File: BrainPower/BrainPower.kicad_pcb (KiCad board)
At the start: 2 copper layers, 149.9 x 111.3 mm, 10 parts, among them J1 BarrelJack_Horizontal, J2 PhoenixContact_MCV_1,5_2-G-5.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, P1 Golden finger, PCIeX1, Dual, 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

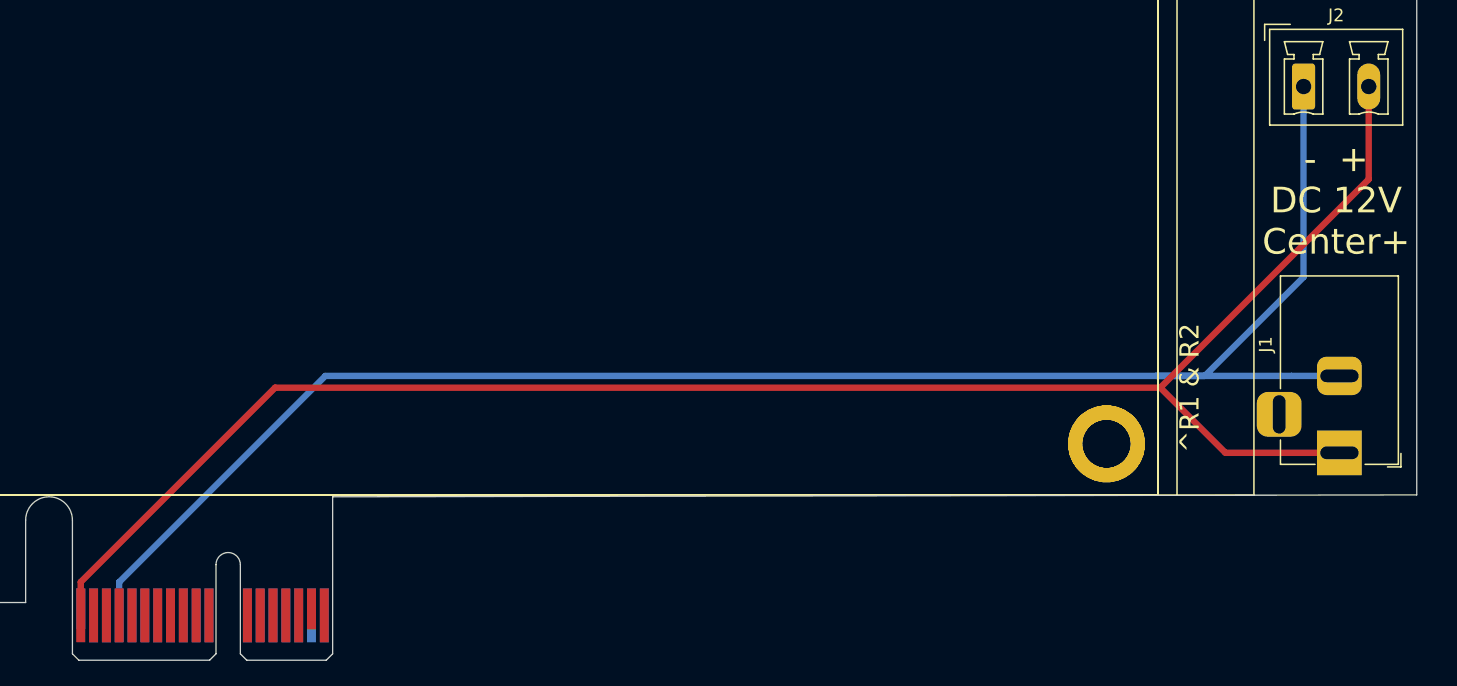
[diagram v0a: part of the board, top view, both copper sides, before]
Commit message: thicker wire
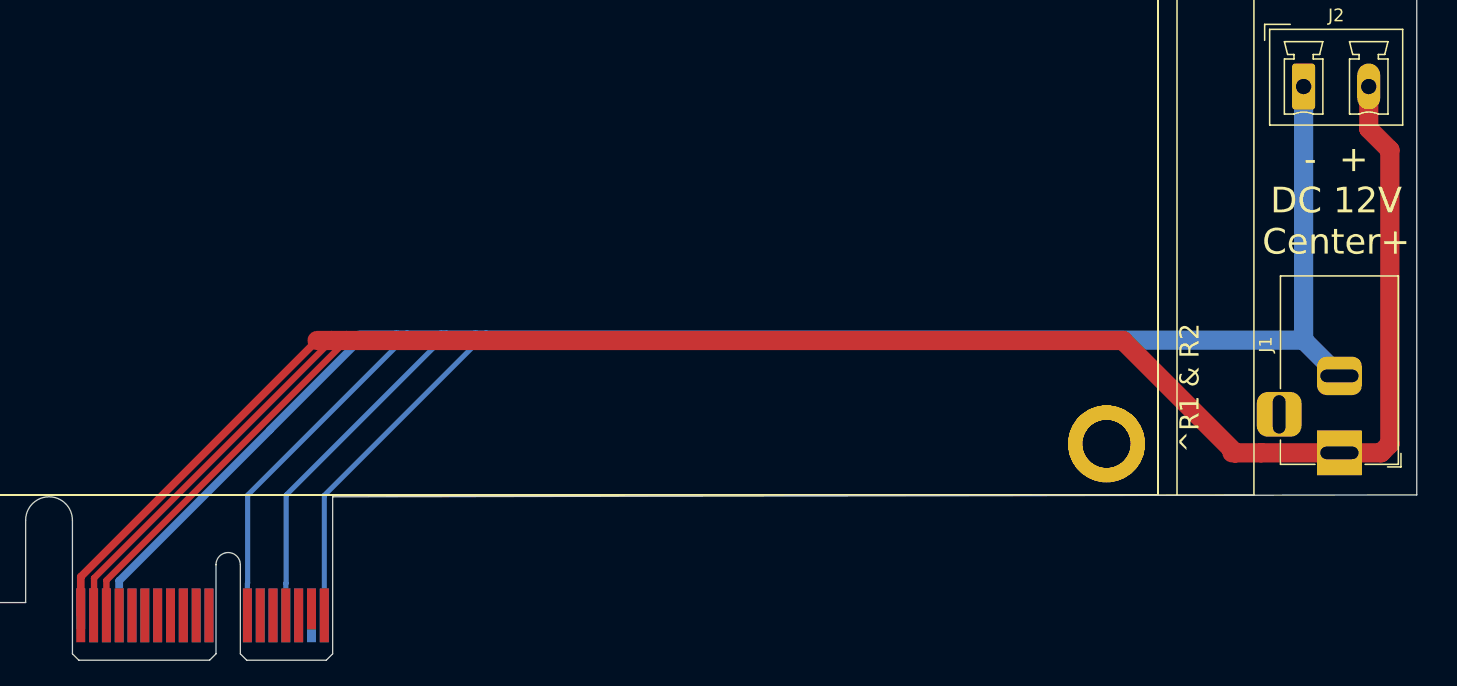
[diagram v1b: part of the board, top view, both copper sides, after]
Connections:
- P1 pad A12: (no net) -> GND
- P1 pad A15: (no net) -> GND
- P1 pad A18: (no net) -> GND
- P1 pad B2: (no net) -> +12V
- P1 pad B3: (no net) -> +12V
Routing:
- net GND: track 134.0 -> 206.8 mm
- net +12V: track 141.2 -> 205.6 mm
